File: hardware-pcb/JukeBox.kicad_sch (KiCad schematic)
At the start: 72 parts, among them J1 USB4105-GF-A, J2 Conn_01x03, J3 Conn_01x04, J4 Conn_01x08, J5 Conn_01x01, J6 Conn_01x03, J7 Conn_01x03, J8 Conn_01x01, SW1 SW_SPST, SW10 SW_SPST, SW11 SW_SPST, SW12 SW_SPST, SW2 SW_SPST, SW3 SW_SPST, SW4 SW_SPST, SW5 SW_SPST, SW6 SW_SPST, SW7 SW_SPST, SW8 SW_SPST, SW9 SW_SPST, U1 NCP1117-3.3_SOT223, U2 W25Q128JVS, U3 RP2040, Y1 ABLS-12.000MHZ-B4-T

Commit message: change mounting holes to M3 from M2.5
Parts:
- H1, H2, H3, H4: footprint MountingHole:MountingHole_2.7mm_M2.5 -> MountingHole:MountingHole_3.2mm_M3
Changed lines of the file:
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@@
       (effects (font (size 1.27 1.27)) (justify left))
     )
-    (property "Footprint" "MountingHole:MountingHole_2.7mm_M2.5" (id 2) (at 279.4 264.16 0)
+    (property "Footprint" "MountingHole:MountingHole_3.2mm_M3" (id 2) (at 279.4 264.16 0)
       (effects (font (size 1.27 1.27)) hide)
     )
@@
       (effects (font (size 1.27 1.27)) (justify left))
     )
-    (property "Footprint" "MountingHole:MountingHole_2.7mm_M2.5" (id 2) (at 279.4 269.24 0)
+    (property "Footprint" "MountingHole:MountingHole_3.2mm_M3" (id 2) (at 279.4 269.24 0)
       (effects (font (size 1.27 1.27)) hide)
     )
@@
       (effects (font (size 1.27 1.27)) (justify left))
     )
-    (property "Footprint" "MountingHole:MountingHole_2.7mm_M2.5" (id 2) (at 279.4 274.32 0)
+    (property "Footprint" "MountingHole:MountingHole_3.2mm_M3" (id 2) (at 279.4 274.32 0)
       (effects (font (size 1.27 1.27)) hide)
     )
@@
       (effects (font (size 1.27 1.27)) (justify left))
     )
-    (property "Footprint" "MountingHole:MountingHole_2.7mm_M2.5" (id 2) (at 279.4 279.4 0)
+    (property "Footprint" "MountingHole:MountingHole_3.2mm_M3" (id 2) (at 279.4 279.4 0)
       (effects (font (size 1.27 1.27)) hide)
     )
@@
     )
     (path "/00000000-0000-0000-0000-00005ef4c292"
-      (reference "H1") (unit 1) (value "MountingHole") (footprint "MountingHole:MountingHole_2.7mm_M2.5")
+      (reference "H1") (unit 1) (value "MountingHole") (footprint "MountingHole:MountingHole_3.2mm_M3")
     )
     (path "/00000000-0000-0000-0000-00005ef4cf1f"
-      (reference "H2") (unit 1) (value "MountingHole") (footprint "MountingHole:MountingHole_2.7mm_M2.5")
+      (reference "H2") (unit 1) (value "MountingHole") (footprint "MountingHole:MountingHole_3.2mm_M3")
     )
     (path "/00000000-0000-0000-0000-00005ef4d323"
-      (reference "H3") (unit 1) (value "MountingHole") (footprint "MountingHole:MountingHole_2.7mm_M2.5")
+      (reference "H3") (unit 1) (value "MountingHole") (footprint "MountingHole:MountingHole_3.2mm_M3")
     )
     (path "/00000000-0000-0000-0000-00005ef4d57b"
-      (reference "H4") (unit 1) (value "MountingHole") (footprint "MountingHole:MountingHole_2.7mm_M2.5")
+      (reference "H4") (unit 1) (value "MountingHole") (footprint "MountingHole:MountingHole_3.2mm_M3")
     )
     (path "/171df43b-a498-4cdb-82fb-17ff4085f303"

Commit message: add more pillars for keyboard frame support, fix footprint for firmware chip
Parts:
- U2: footprint Package_SO:SOIC-8_5.23x5.23mm_P1.27mm -> Package_SO:SOIC-8_3.9x4.9mm_P1.27mm
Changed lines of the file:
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@@
     (property "Reference" "U2" (id 0) (at 40.64 99.06 0))
     (property "Value" "W25Q128JVS" (id 1) (at 54.61 119.38 0))
-    (property "Footprint" "Package_SO:SOIC-8_5.23x5.23mm_P1.27mm" (id 2) (at 46.99 109.22 0)
+    (property "Footprint" "Package_SO:SOIC-8_3.9x4.9mm_P1.27mm" (id 2) (at 46.99 109.22 0)
       (effects (font (size 1.27 1.27)) hide)
     )
@@
     )
     (path "/00000000-0000-0000-0000-00005eda5f2c"
-      (reference "U2") (unit 1) (value "W25Q128JVS") (footprint "Package_SO:SOIC-8_5.23x5.23mm_P1.27mm")
+      (reference "U2") (unit 1) (value "W25Q128JVS") (footprint "Package_SO:SOIC-8_3.9x4.9mm_P1.27mm")
     )
     (path "/00000000-0000-0000-0000-00005ed8f5d6"

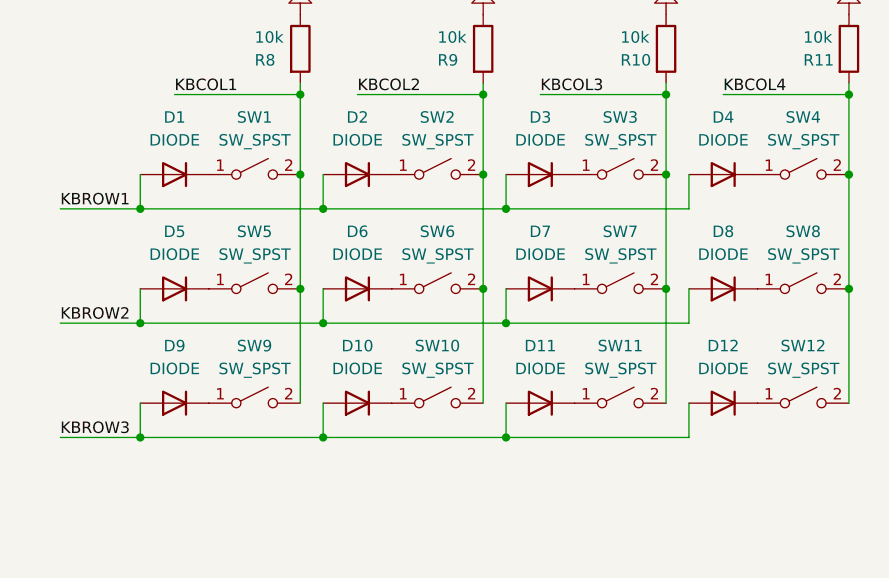
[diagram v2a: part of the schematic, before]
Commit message: fix keyboard diode direction
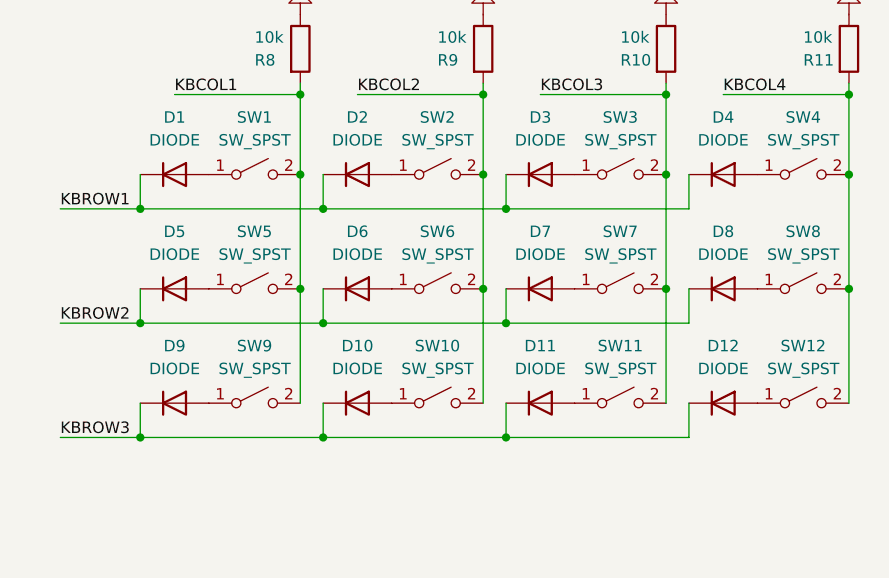
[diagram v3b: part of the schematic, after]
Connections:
- net GPIO10: now also D5.2 (K), D6.2 (K), D7.2 (K), D8.2 (K); no longer D5.1 (A), D6.1 (A), D7.1 (A), D8.1 (A)
- net GPIO11: now also D10.2 (K), D11.2 (K), D12.2 (K), D9.2 (K); no longer D10.1 (A), D11.1 (A), D12.1 (A), D9.1 (A)
- net GPIO9: now also D1.2 (K), D2.2 (K), D3.2 (K), D4.2 (K); no longer D1.1 (A), D2.1 (A), D3.1 (A), D4.1 (A)
- net at SW11.1 (A): now also D11.1 (A); no longer D11.2 (K)
- net at SW7.1 (A): now also D7.1 (A); no longer D7.2 (K)
- net at SW9.1 (A): now also D9.1 (A); no longer D9.2 (K)
- net at SW4.1 (A): now also D4.1 (A); no longer D4.2 (K)
- net at SW8.1 (A): now also D8.1 (A); no longer D8.2 (K)
- net at SW10.1 (A): now also D10.1 (A); no longer D10.2 (K)
- net at SW2.1 (A): now also D2.1 (A); no longer D2.2 (K)
- net at SW3.1 (A): now also D3.1 (A); no longer D3.2 (K)
- net at SW6.1 (A): now also D6.1 (A); no longer D6.2 (K)
- net at SW1.1 (A): now also D1.1 (A); no longer D1.2 (K)
- net at SW5.1 (A): now also D5.1 (A); no longer D5.2 (K)
- net at SW12.1 (A): now also D12.1 (A); no longer D12.2 (K)
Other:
- moved on the sheet: D1, D10, D11, D12, D2, D3, D4, D5, D6, D7, D8, D9

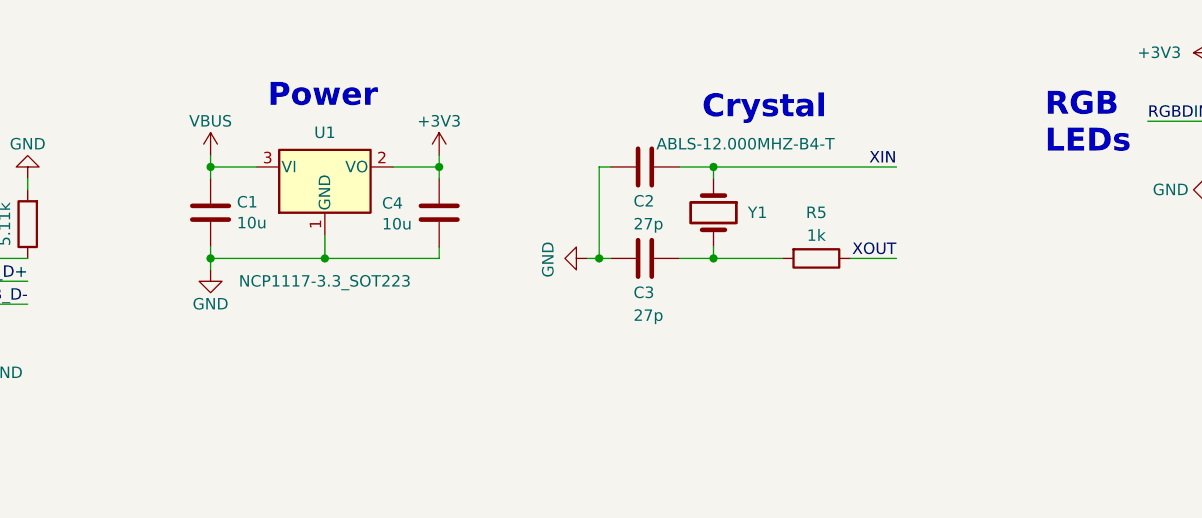
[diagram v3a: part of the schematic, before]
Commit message: add smaller clock crystal, with adjusted capacitor values
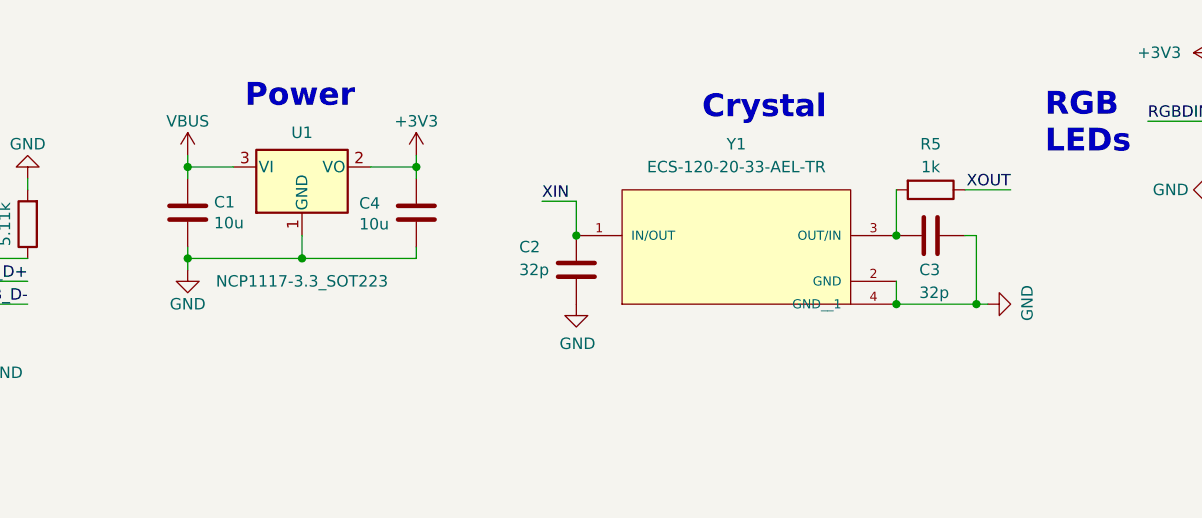
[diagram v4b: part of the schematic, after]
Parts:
- removed Y1: ABLS-12.000MHZ-B4-T, RP2040_minimal:Crystal_SMD_HC49-US, symbol Device:Crystal
- added Y1: ECS-120-20-33-AEL-TR, RP2040_minimal:XTAL_ECS-120-20-33-AEL-TR, symbol ECS-120-20-33-AEL-TR:ECS-120-20-33-AEL-TR
- C2, C3: value 27p -> 32p
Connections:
- net GND: now also C3.1, Y1.2 (GND), Y1.4 (GND__1); no longer C3.2
- net XIN: now also Y1.1 (IN/OUT)
- net at R5.2: now also C3.2, Y1.3 (OUT/IN); no longer C3.1
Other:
- moved on the sheet: C1, C2, C3, C4, R5, U1

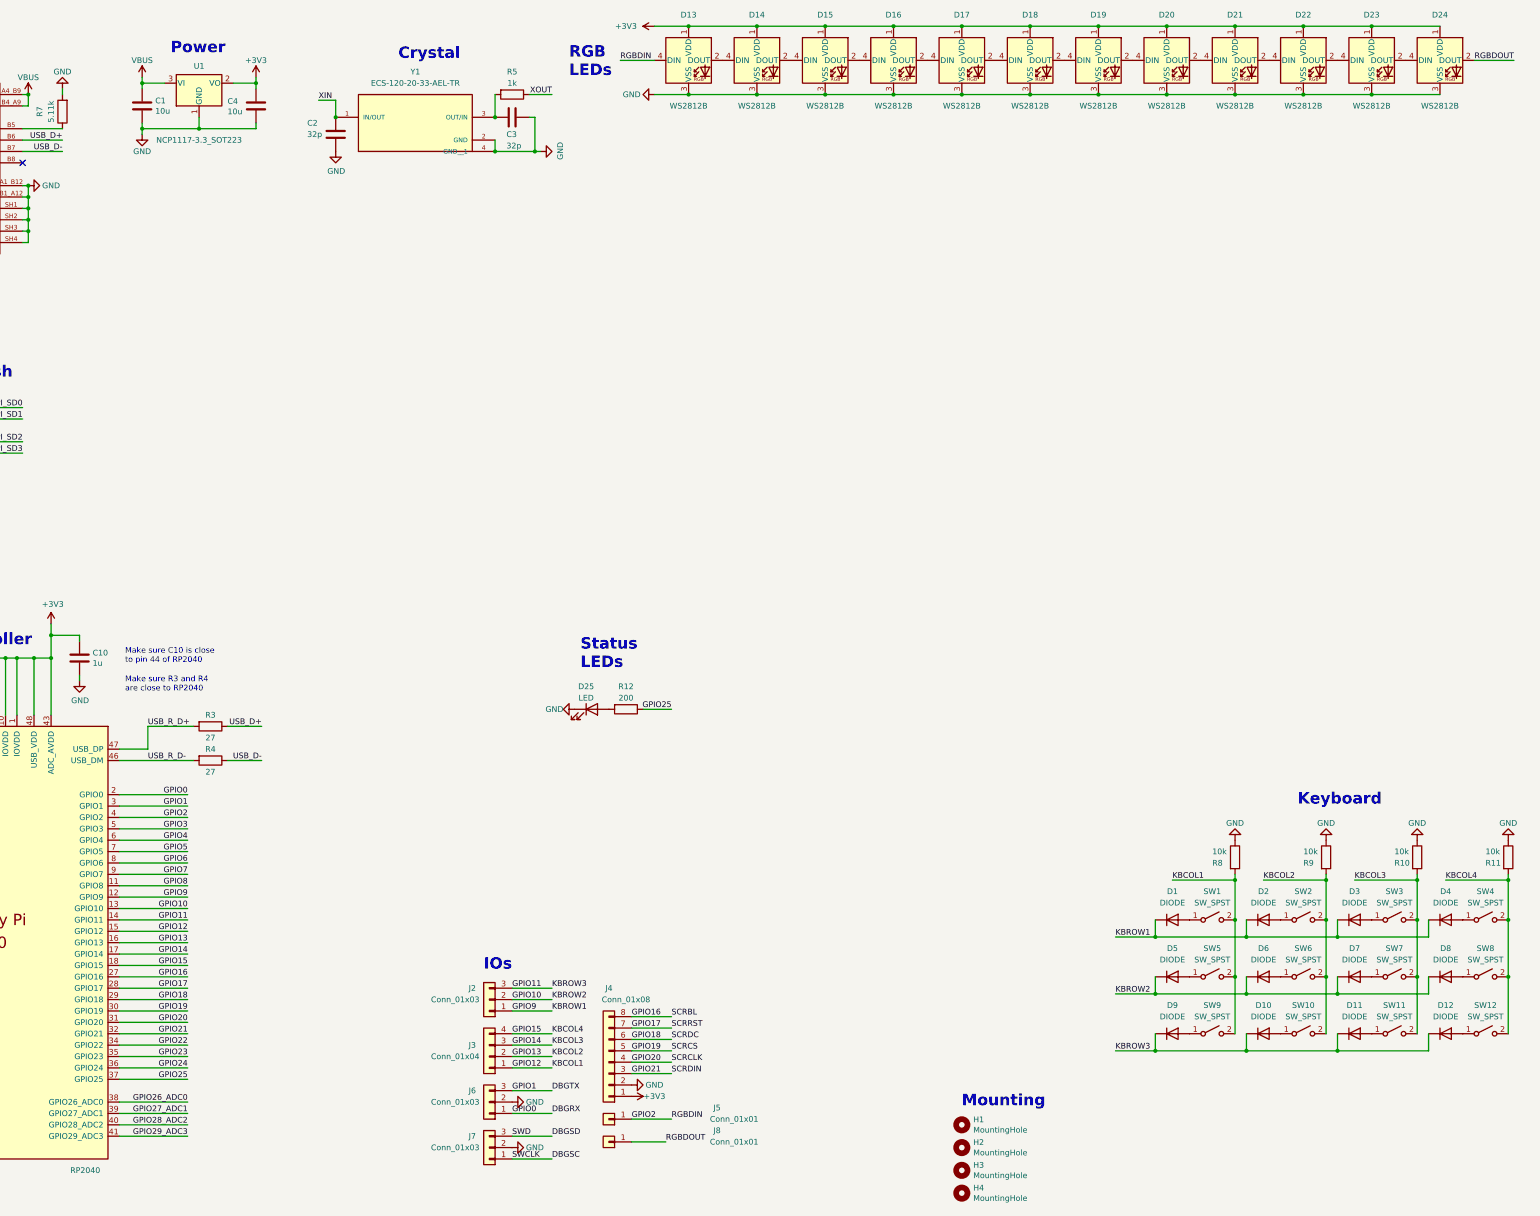
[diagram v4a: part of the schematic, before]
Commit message: change throughhole pins to test pads, start reassembling pcb
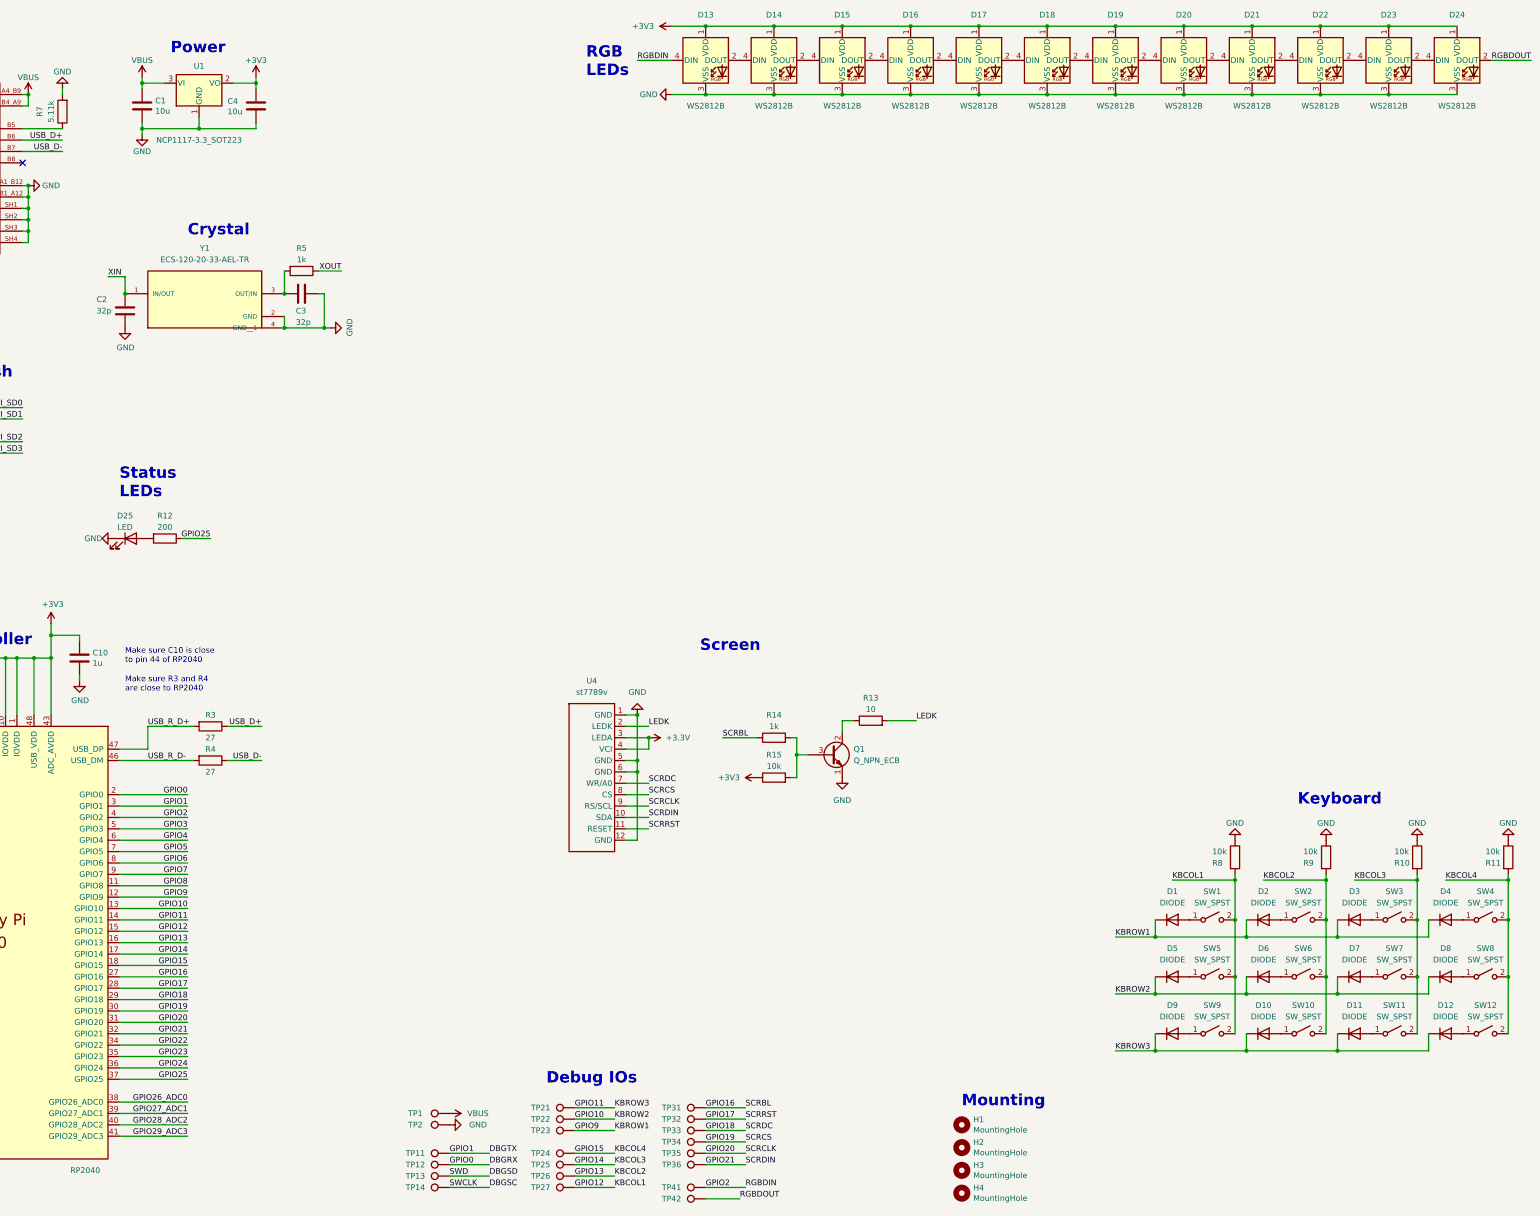
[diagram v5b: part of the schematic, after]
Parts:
- removed J2, J6, J7: Conn_01x03, Connector_PinHeader_2.54mm:PinHeader_1x03_P2.54mm_Vertical, symbol Connector_Generic:Conn_01x03
- removed J3: Conn_01x04, Connector_PinHeader_2.54mm:PinHeader_1x04_P2.54mm_Vertical, symbol Connector_Generic:Conn_01x04
- removed J4: Conn_01x08, Connector_PinHeader_2.54mm:PinHeader_1x08_P2.54mm_Vertical, symbol Connector_Generic:Conn_01x08
- removed J5, J8: Conn_01x01, Connector_PinHeader_2.54mm:PinHeader_1x01_P2.54mm_Vertical, symbol Connector_Generic:Conn_01x01
- added Q1: Q_NPN_ECB, Package_TO_SOT_SMD:SOT-23, symbol Device:Q_NPN_ECB
- added R13: 10, Resistor_SMD:R_0805_2012Metric_Pad1.20x1.40mm_HandSolder, symbol Device:R
- added R14: 1k, Resistor_SMD:R_0805_2012Metric_Pad1.20x1.40mm_HandSolder, symbol Device:R
- added R15: 10k, Resistor_SMD:R_0805_2012Metric_Pad1.20x1.40mm_HandSolder, symbol Device:R
- added TP1, TP11, TP12, TP13, TP14, TP2, TP21, TP22, TP23, TP24, TP25, TP26, TP27, TP31, TP32, TP33, TP34, TP35, TP36, TP41, TP42: TestPoint, TestPoint:TestPoint_Pad_D4.0mm, symbol Connector:TestPoint
- added U4: st7789v, RP2040_minimal:st7789v, symbol st7789v:st7789v
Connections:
- net +3V3: now also R15.1
- net DBGRX: now also TP12.1
- net DBGSC: now also TP14.1
- net DBGSD: now also TP13.1
- net DBGTX: now also TP11.1
- net GND: now also Q1.1 (E), TP2.1, U4.1 (GND), U4.12 (GND), U4.5 (GND), U4.6 (GND)
- net GPIO10: now also TP22.1
- net GPIO11: now also TP21.1
- net GPIO12: now also TP27.1
- net GPIO13: now also TP26.1
- net GPIO14: now also TP25.1
- net GPIO15: now also TP24.1
- net GPIO16: now also R14.1, TP31.1
- net GPIO17: now also TP32.1, U4.11 (RESET)
- net GPIO18: now also TP33.1, U4.7 (WR/A0)
- net GPIO19: now also TP34.1, U4.8 (CS)
- net GPIO2: now also TP41.1
- net GPIO20: now also TP35.1, U4.9 (RS/SCL)
- net GPIO21: now also TP36.1, U4.10 (SDA)
- net GPIO9: now also TP23.1
- net RGBDOUT: now also TP42.1
- net VBUS: now also TP1.1
- new net: Q1.2 (C), R13.1
- new net: Q1.3 (B), R14.2, R15.2
- new net +3.3V: U4.3 (LEDA), U4.4 (VCI)
- new net LEDK: R13.2, U4.2 (LEDK)
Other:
- note added: "Debug IOs"
- note added: "Screen"
- note removed: "IOs"
- moved on the sheet: C2, C3, D13, D14, D15, D16, D17, D18, D19, D20, D21, D22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

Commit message: update to kicad 8
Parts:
- D1, D10, D11, D12, D2, D3, D4, D5, D6, D7, D8, D9: value DIODE -> ${SIM.PARAMS}; Spice_Netlist_Enabled Y -> (none); Spice_Primitive D -> (none)
